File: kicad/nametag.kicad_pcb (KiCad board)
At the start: 4 copper layers, 78 x 36 mm, 84 parts, among them J2 FPC24 0.5mm, J3 Prog Header, Q1 Si1308EDL, Q2 AO3401A, Q3 AO3401A, SW2 SW_Push, U2 nRF52832-QFxx, Y2 Crystal_GND24

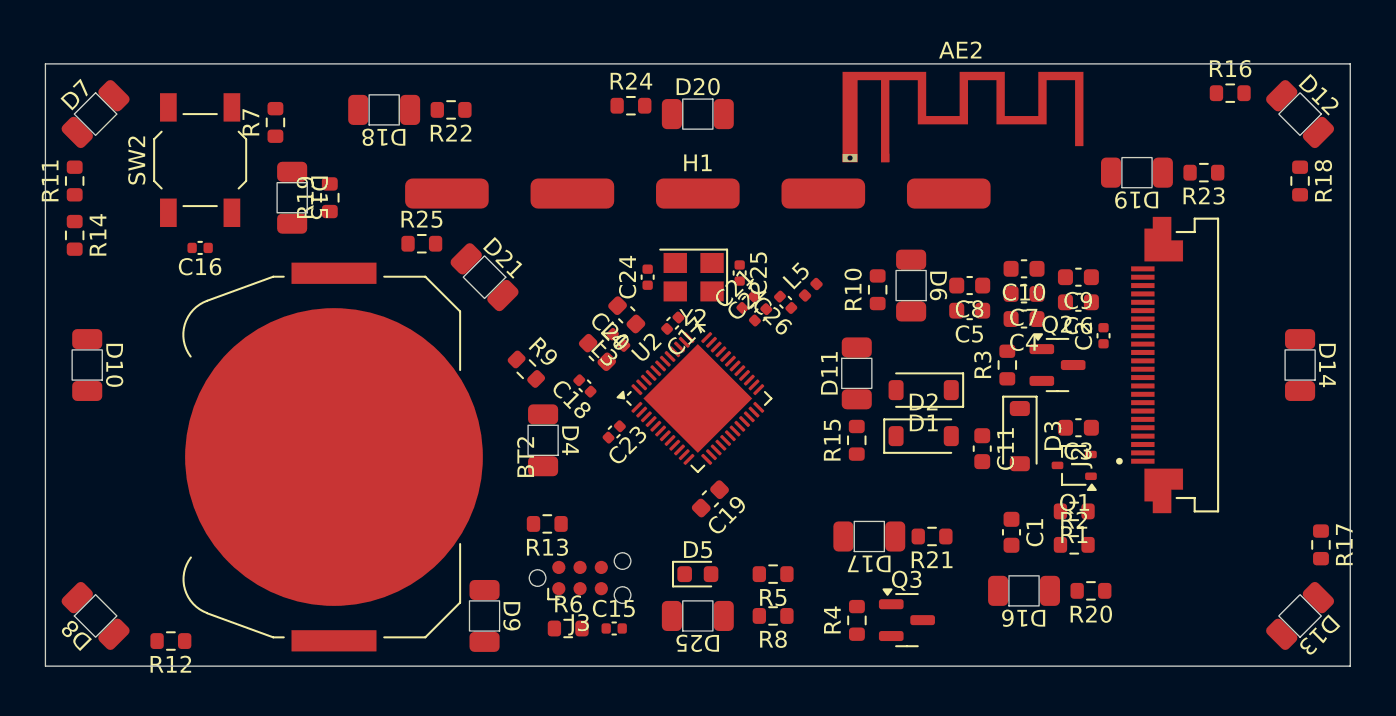
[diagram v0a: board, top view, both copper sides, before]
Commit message: First routing
Did the routing for everything and made it somewhat useable.
Have to sleep again for a night to see if I want to do it like this.
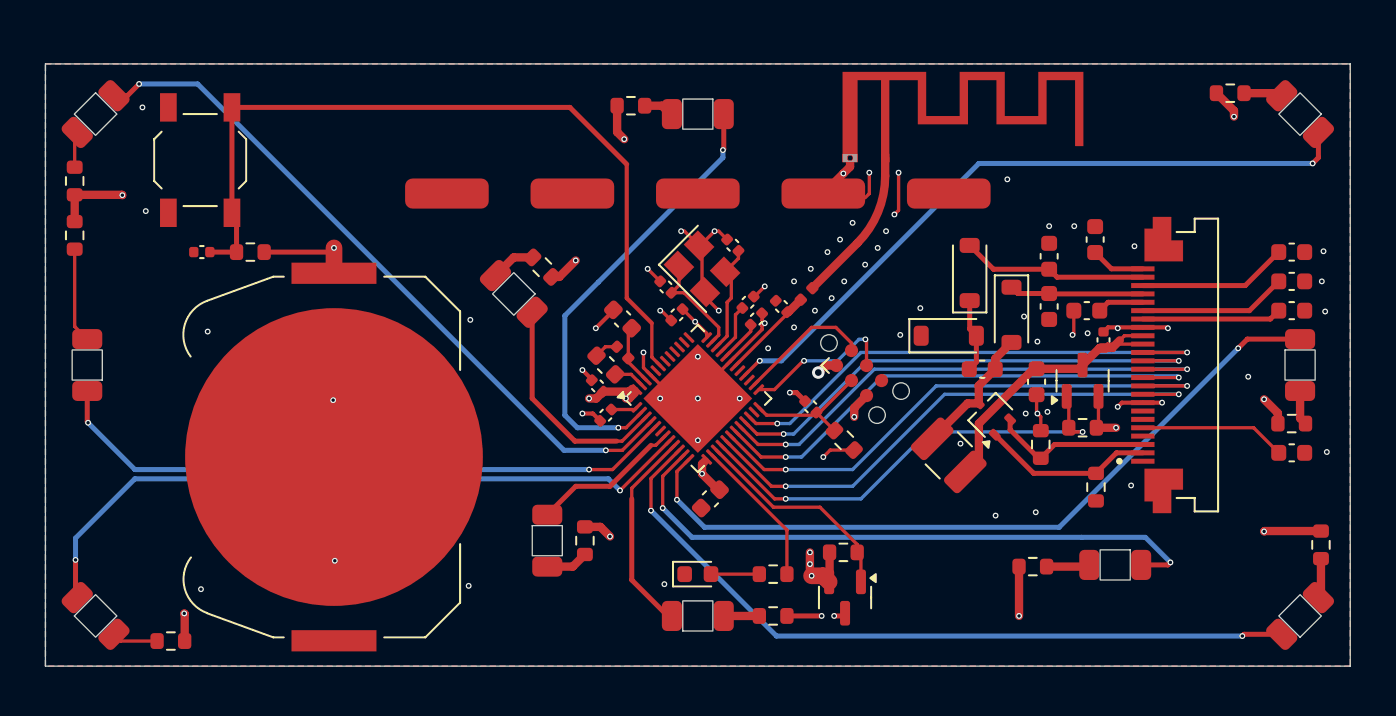
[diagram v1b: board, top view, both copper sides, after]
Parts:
- removed D11, D15, D16, D17, D18, D19, D21: LED, g-LED_SMD:LTST-C230
- removed R15, R19, R20, R21, R22, R23, R25: R, Resistor_SMD:R_0603_1608Metric
- added L1: 68uH, Inductor_SMD:L_1210_3225Metric, F.Cu at (154.0, 98.4)
- moved D4 35.0 mm to (163.9, 105.0), turned to -90 degrees
- moved R9 32.5 mm to (159.0, 105.0), turned to 0 degrees
- moved D6 26.6 mm to (130.0, 103.5), turned to 0 degrees
- moved R10 23.0 mm to (132.2, 103.5), turned to -90 degrees
- moved J3 20.7 mm to (148.6, 93.5), turned to -45 degrees
- moved R6 20.0 mm to (147.8, 97.5), turned to 135 degrees
- moved C8 19.4 mm to (174.5, 86.2), turned to 0 degrees
- moved C5 19.3 mm to (174.5, 88.0), turned to 0 degrees
- moved D9 19.3 mm to (128.0, 88.8), turned to -135 degrees
- moved C15 17.7 mm to (145.8, 95.5), turned to 135 degrees
- moved C4 16.0 mm to (174.5, 89.8), turned to 0 degrees
- moved R13 15.4 mm to (129.7, 87.2), turned to 135 degrees
- moved R18 14.5 mm to (174.5, 96.5), turned to 0 degrees
- moved C3 12.8 mm to (174.5, 98.2), turned to 0 degrees
- moved C1 9.12 mm to (159.2, 94.0)
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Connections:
- D6 pad 1: LED_3 -> LED_8
- J3 pad 6: SWO -> unconnected-(J3-SWO-Pad6)
- U2 pad 10: unconnected-(U2-P0.08-Pad10) -> LED_10
- U2 pad 11: unconnected-(U2-NFC1/P0.09-Pad11) -> LED_2
- U2 pad 12: unconnected-(U2-NFC2/P0.10-Pad12) -> LED_11
- U2 pad 14: unconnected-(U2-P0.11-Pad14) -> LED
- U2 pad 15: unconnected-(U2-P0.12-Pad15) -> LED-POWER
- U2 pad 16: unconnected-(U2-P0.13-Pad16) -> ENABLE
- U2 pad 17: BUTTON -> BUSY
- U2 pad 18: unconnected-(U2-P0.15-Pad18) -> eP_RESET
- U2 pad 19: LED -> DATA/CLOCK
- U2 pad 2: unconnected-(U2-P0.00/XL1-Pad2) -> LED_17
- U2 pad 20: unconnected-(U2-P0.17-Pad20) -> CS
- U2 pad 21: unconnected-(U2-P0.18/SWO-Pad21) -> SCK
- U2 pad 22: unconnected-(U2-P0.19-Pad22) -> SDI
- U2 pad 28: unconnected-(U2-P0.23-Pad28) -> LED_9
- U2 pad 3: unconnected-(U2-P0.01/XL2-Pad3) -> LED_6
- U2 pad 4: unconnected-(U2-P0.02/AIN0-Pad4) -> LED_4
- U2 pad 43: unconnected-(U2-P0.31/AIN7-Pad43) -> BUTTON
- U2 pad 5: unconnected-(U2-P0.03/AIN1-Pad5) -> LED_7
- U2 pad 7: unconnected-(U2-P0.05/AIN3-Pad7) -> LED_8
- U2 pad 8: unconnected-(U2-P0.06-Pad8) -> LED_5
- U2 pad 9: unconnected-(U2-P0.07-Pad9) -> LED_1
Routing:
- net VLED: track 0.00 -> 232.7 mm, vias 0 -> 11
- net VCC: track 0.00 -> 117.0 mm, vias 0 -> 11
- net BUTTON: track 0.00 -> 48.3 mm
- net GND: track 0.00 -> 46.4 mm, vias 0 -> 70
- net LED_11: track 0.00 -> 45.3 mm, vias 0 -> 2
- net LED_10: track 0.00 -> 45.2 mm, vias 0 -> 2
- net LED_4: track 0.00 -> 42.2 mm, vias 0 -> 2
- net LED_5: track 0.00 -> 42.1 mm, vias 0 -> 2
- net LED_9: track 0.00 -> 41.2 mm, vias 0 -> 2
- net LED_7: track 0.00 -> 38.1 mm, vias 0 -> 2
- net LED_2: track 0.00 -> 37.2 mm, vias 0 -> 2
- net eP_RESET: track 0.00 -> 32.9 mm, vias 0 -> 2
- net BUSY: track 0.00 -> 32.7 mm, vias 0 -> 2
- net CS: track 0.00 -> 31.7 mm, vias 0 -> 2
- net DATA/CLOCK: track 0.00 -> 31.4 mm, vias 0 -> 2
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- added copper zone on B.Cu, net GND
- added copper zone on F.Cu, net GND
- added copper zone on In1.Cu, net GND
